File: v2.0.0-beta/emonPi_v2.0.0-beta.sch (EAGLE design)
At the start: 79 parts, among them IC1 AVR128DB32-I_PT, IC2 MCP1501-10E_SN, J1 SJ-3524-SMT-TR, J2 SJ-3524-SMT-TR, J4 SJ-3524-SMT-TR, J9 RJ11, Y1 MCSJK-7U-12.00-12-10-80-B-10

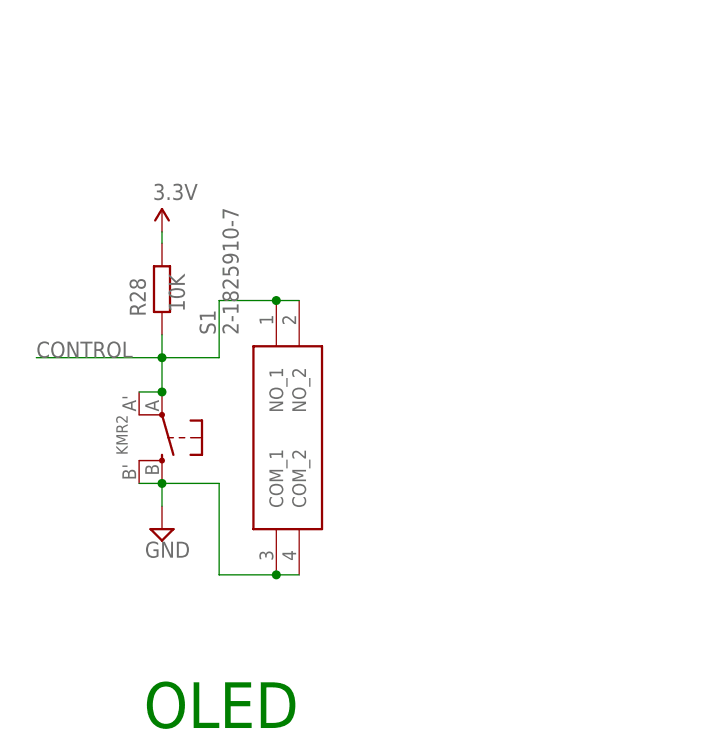
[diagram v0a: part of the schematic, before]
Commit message: fix push switch
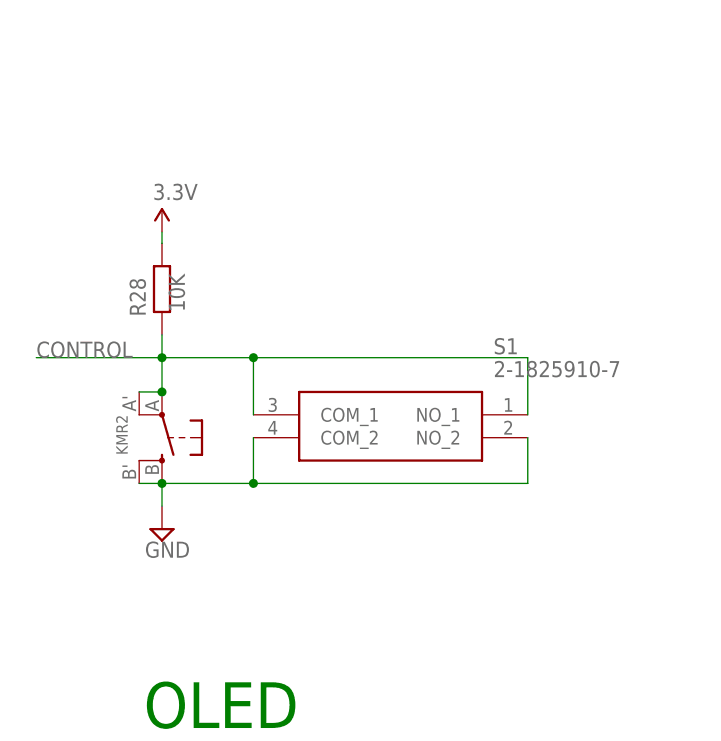
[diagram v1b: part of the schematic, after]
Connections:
- net CONTROL: now also S1.COM_1; no longer S1.NO_2
- net GND: now also S1.NO_2; no longer S1.COM_1
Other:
- moved on the sheet: S1
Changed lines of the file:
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@@
 <setting verticaltext="up"/>
 </settings>
-<grid distance="0.1" unitdist="inch" unit="inch" style="lines" multiple="1" display="no" altdistance="0.01" altunitdist="inch" altunit="inch"/>
+<grid distance="0.05" unitdist="inch" unit="inch" style="lines" multiple="1" display="no" altdistance="0.01" altunitdist="inch" altunit="inch"/>
 <layers>
 <layer number="1" name="Top" color="4" fill="1" visible="no" active="no"/>
@@
 <attribute name="VALUE" x="105.41" y="280.67" size="1.778" layer="96"/>
 </instance>
-<instance part="S1" gate="G$1" x="308.61" y="166.37" smashed="yes" rot="R90">
-<attribute name="NAME" x="300.99" y="193.04" size="1.778" layer="95" rot="R90" align="center-left"/>
-<attribute name="VALUE" x="303.53" y="193.04" size="1.778" layer="96" rot="R90" align="center-left"/>
+<instance part="S1" gate="G$1" x="306.07" y="184.15" smashed="yes">
+<attribute name="NAME" x="332.74" y="191.77" size="1.778" layer="95" align="center-left"/>
+<attribute name="VALUE" x="332.74" y="189.23" size="1.778" layer="96" align="center-left"/>
 </instance>
 <instance part="JP3" gate="G$1" x="118.11" y="242.57" smashed="yes" rot="R180">
@@
 <wire x1="295.91" y1="176.53" x2="295.91" y2="173.99" width="0.1524" layer="91"/>
 <junction x="295.91" y="176.53"/>
-<pinref part="S1" gate="G$1" pin="COM_1"/>
+<wire x1="306.07" y1="176.53" x2="295.91" y2="176.53" width="0.1524" layer="91"/>
 <pinref part="S1" gate="G$1" pin="COM_2"/>
-<wire x1="308.61" y1="166.37" x2="311.15" y2="166.37" width="0.1524" layer="91"/>
-<wire x1="308.61" y1="166.37" x2="302.26" y2="166.37" width="0.1524" layer="91"/>
-<wire x1="302.26" y1="166.37" x2="302.26" y2="176.53" width="0.1524" layer="91"/>
-<junction x="308.61" y="166.37"/>
-<wire x1="302.26" y1="176.53" x2="295.91" y2="176.53" width="0.1524" layer="91"/>
+<wire x1="306.07" y1="181.61" x2="306.07" y2="176.53" width="0.1524" layer="91"/>
+<pinref part="S1" gate="G$1" pin="NO_2"/>
+<wire x1="336.55" y1="181.61" x2="336.55" y2="176.53" width="0.1524" layer="91"/>
+<wire x1="336.55" y1="176.53" x2="306.07" y2="176.53" width="0.1524" layer="91"/>
+<junction x="306.07" y="176.53"/>
 </segment>
 <segment>
@@
 <wire x1="295.91" y1="190.5" x2="281.94" y2="190.5" width="0.1524" layer="91"/>
 <junction x="295.91" y="190.5"/>
+<pinref part="S1" gate="G$1" pin="COM_1"/>
+<wire x1="306.07" y1="190.5" x2="295.91" y2="190.5" width="0.1524" layer="91"/>
+<wire x1="306.07" y1="190.5" x2="306.07" y2="184.15" width="0.1524" layer="91"/>
 <pinref part="S1" gate="G$1" pin="NO_1"/>
-<pinref part="S1" gate="G$1" pin="NO_2"/>
-<wire x1="308.61" y1="196.85" x2="311.15" y2="196.85" width="0.1524" layer="91"/>
-<wire x1="308.61" y1="196.85" x2="302.26" y2="196.85" width="0.1524" layer="91"/>
-<wire x1="302.26" y1="196.85" x2="302.26" y2="190.5" width="0.1524" layer="91"/>
-<junction x="308.61" y="196.85"/>
-<wire x1="302.26" y1="190.5" x2="295.91" y2="190.5" width="0.1524" layer="91"/>
-</segment>
-<segment>
+<wire x1="306.07" y1="190.5" x2="336.55" y2="190.5" width="0.1524" layer="91"/>
+<wire x1="336.55" y1="190.5" x2="336.55" y2="184.15" width="0.1524" layer="91"/>
+<junction x="306.07" y="190.5"/>
+</segment>
+<segment>
